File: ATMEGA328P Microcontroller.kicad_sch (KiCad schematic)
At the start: 25 parts, among them U1 24LC1025, U2 24LC1025, U3 ATmega328-P, U4 DS1337S_T_R, Y1 32.768 kHz, Y2 16MHz

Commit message: Wiring complete
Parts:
- BT1: footprint Connector_PinHeader_2.54mm:PinHeader_1x02_P2.54mm_Vertical -> (none)
- C1, C2, C3, C4, C5: footprint Capacitor_SMD:C_0805_2012Metric_Pad1.18x1.45mm_HandSolder -> (none)
- D1, D2: footprint LED_SMD:LED_0805_2012Metric -> (none)
- H1, H2, H3, H4: footprint MountingHole:MountingHole_2.1mm -> (none)
- R: renamed from R5; footprint Resistor_SMD:R_0805_2012Metric -> (none)
- R1, R2, R3, R4, R6, R7: footprint Resistor_SMD:R_0805_2012Metric -> (none)
- U1, U2: footprint Package_SO:SOIC-8_5.23x5.23mm_P1.27mm -> (none)
- Y1, Y2: footprint Crystal:Crystal_SMD_5032-2Pin_5.0x3.2mm_HandSoldering -> (none)
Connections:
- net GND: now also BT1.2 (-), C1.1, C2.1, C3.2, C4.2, C5.2, R.1, R4.2, U2.2 (A1), U2.4 (GND), U2.7 (WP), U3.22 (GND), U3.8 (GND)
- net at D1.1 (K): now also R.2
- net SCK: now reaches D1.2 (A)
- net SCK: now also R1.2, U1.6 (SCL), U2.6 (SCL), U3.19 (PB5), U3.28 (PC5), U4.6 (SCL)
- net Vcc: now reaches R1.1
- net Vcc: now also C3.1, R2.1, R3.1, R6.1, R7.1, U1.1 (A0), U1.2 (A1), U1.3 (A2), U1.8 (VCC), U2.1 (A0), U2.3 (A2), U2.8 (VCC), U4.8 (VCC)
- net at C1.2: now also U3.9 (XTAL1/PB6), Y2.1
- net SDA: now reaches U1.5 (SDA)
- net SDA: now also R2.2, U2.5 (SDA), U3.27 (PC4), U4.5 (SDA)
- net at D2.1 (K): now also R4.1
- net at D2.2 (A): now also BT1.1 (+), C5.1, U3.20 (AVCC), U3.7 (VCC)
- net at R6.2: now also U4.7 (SQW/~INT)
- net at Y2.2: now also C2.2, U3.10 (XTAL2/PB7)
- net at C4.1: now also U3.21 (AREF)
- net at U4.3 (~{INTA}): now also R3.2
- net RESET: now reaches R7.2
- net RESET: now also U3.1 (~{RESET}/PC6)
- net D4: now reaches U3.11 (PD5)
- net D5: now reaches U3.12 (PD6)
- net D6: now reaches U3.13 (PD7)
- net D7: now reaches U3.14 (PB0)
- net MOSI: now reaches U3.17 (PB3)
- net MISO: now reaches U3.18 (PB4)
- net RX: now reaches U3.2 (PD0)
- net TX: now reaches U3.3 (PD1)
- net D1: now reaches U3.4 (PD2)
- net D2: now reaches U3.5 (PD3)
- net D3: now reaches U3.6 (PD4)
- no-connect marks 0 -> 6
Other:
- moved on the sheet: BT1, C1, C2, C3, C4, C5, D1, D2, R, R3, R4, R6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

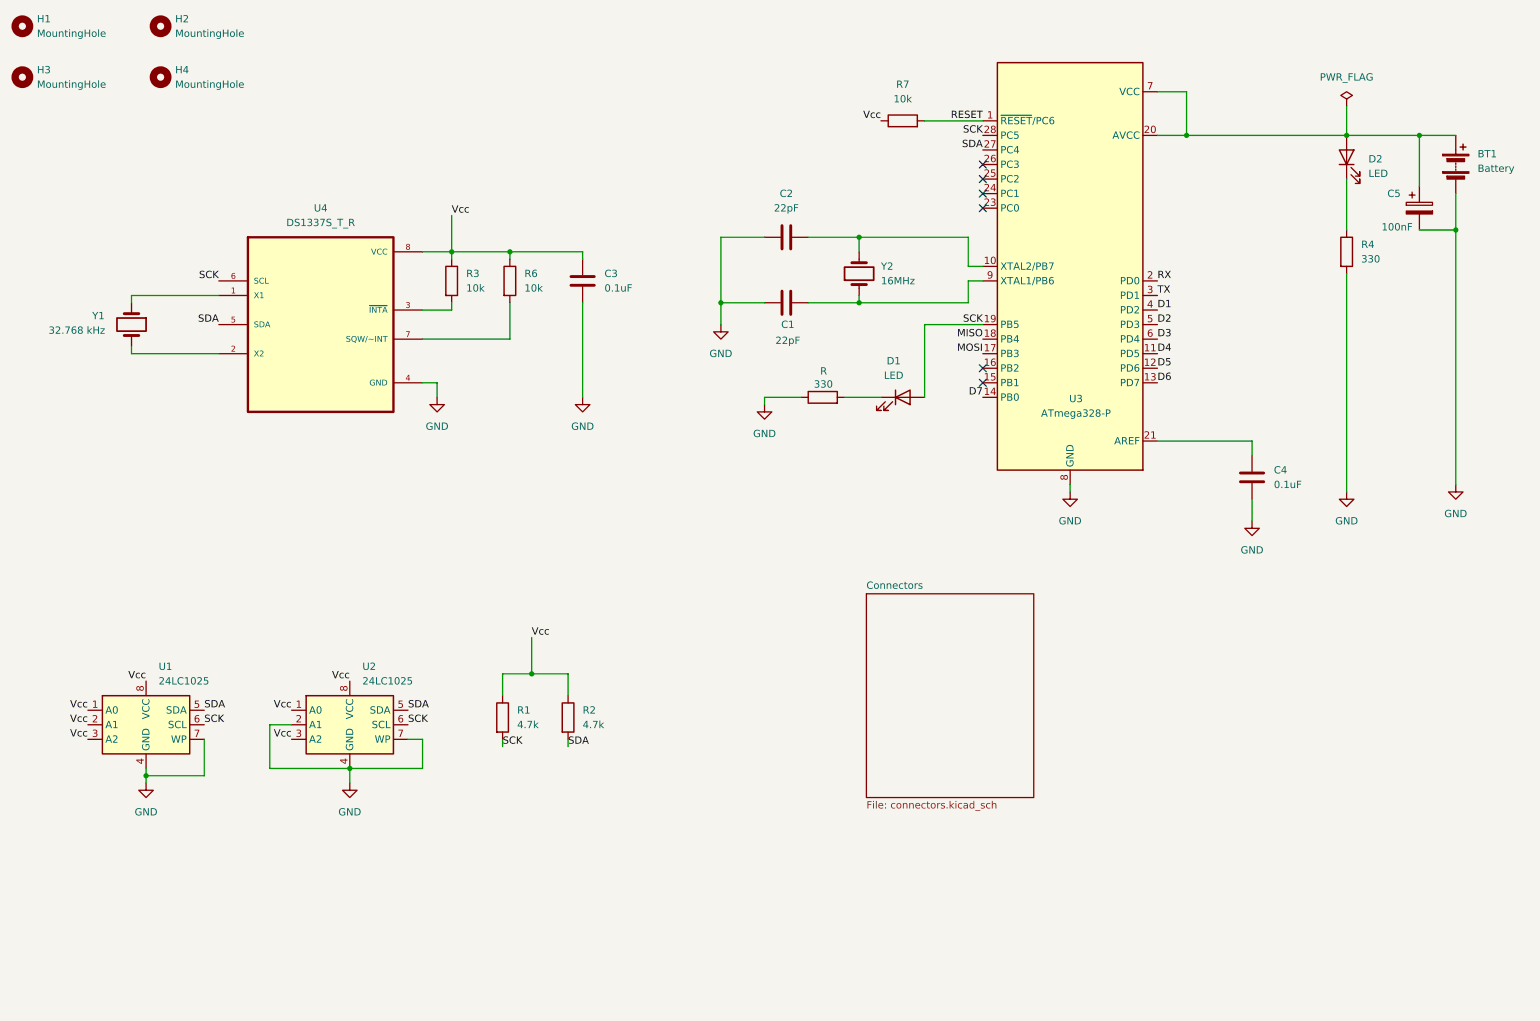
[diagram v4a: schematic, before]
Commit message: Allocated Vcc and GND nets to Power netclass
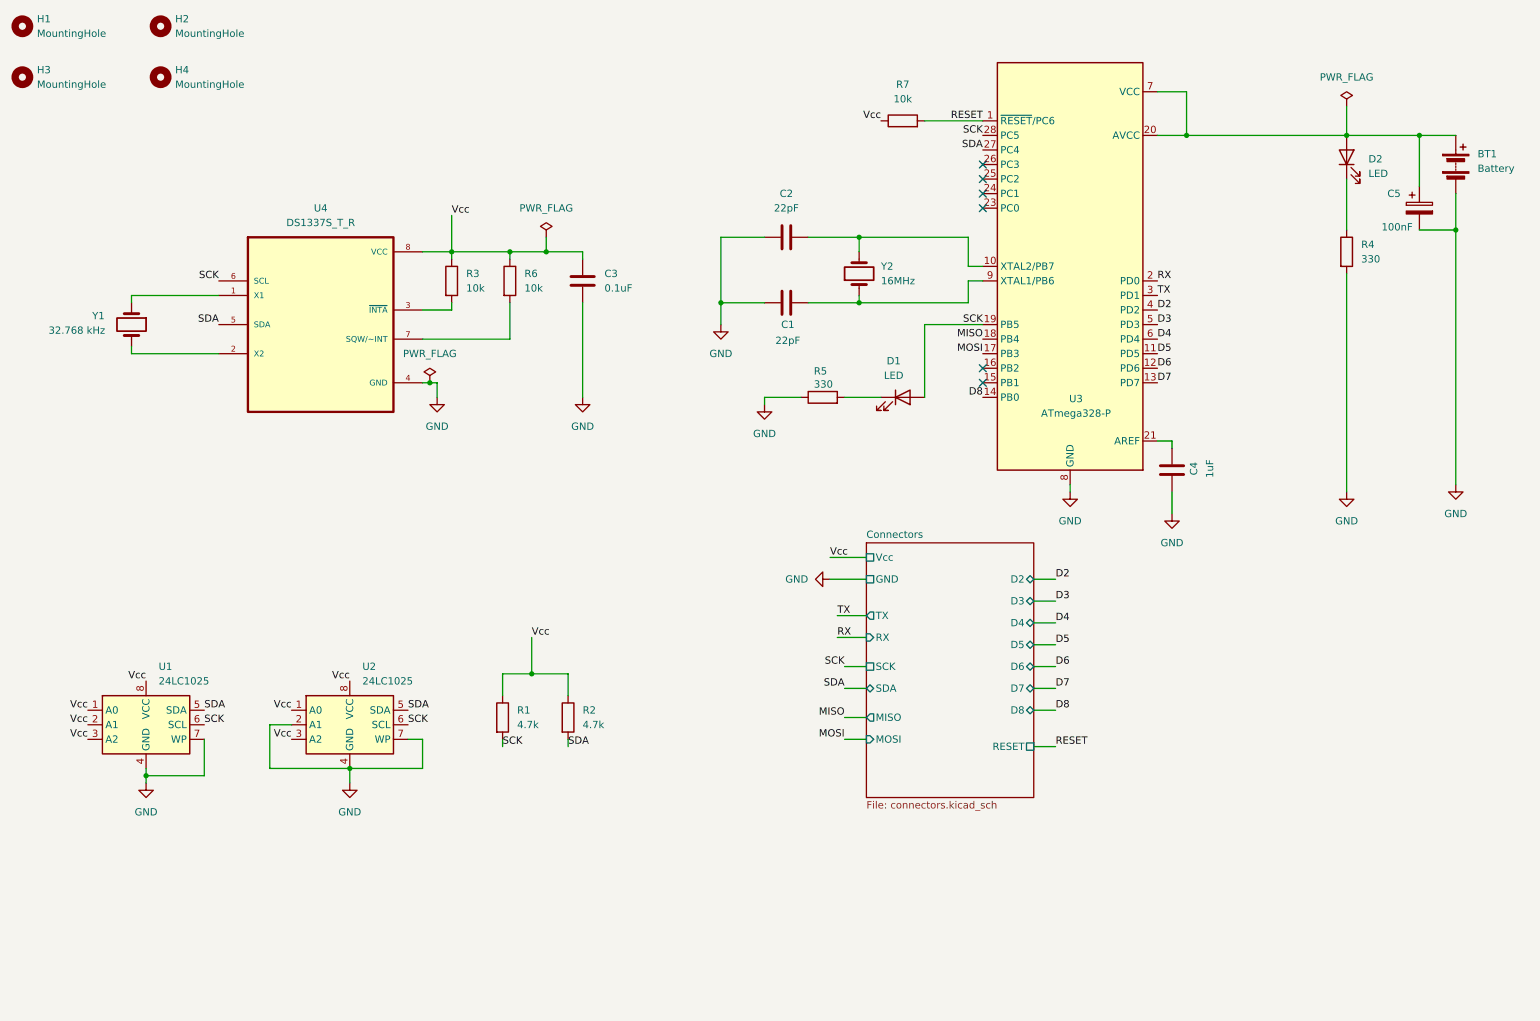
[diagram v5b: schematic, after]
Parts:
- C4: value 0.1uF -> 1uF
- renumbered R to R5
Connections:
- net D1 is gone; now on net D2: U3.4 (PD2)
- net D2: no longer U3.5 (PD3)
- net D3: now also U3.5 (PD3); no longer U3.6 (PD4)
- net D4: now also U3.6 (PD4); no longer U3.11 (PD5)
- net D5: now also U3.11 (PD5); no longer U3.12 (PD6)
- net D6: now also U3.12 (PD6); no longer U3.13 (PD7)
- net D7: now also U3.13 (PD7); no longer U3.14 (PB0)
- net GND: now also C4.1; no longer C4.2
- net at U3.21 (AREF): now also C4.2; no longer C4.1
- new net D8: U3.14 (PB0)
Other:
- sheet Connectors ports: added D2, D3, D4, D5, D6, D7, D8, GND, MISO, MOSI, RESET, RX, SCK, SDA, TX, Vcc; removed none

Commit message: Added comments to schematic
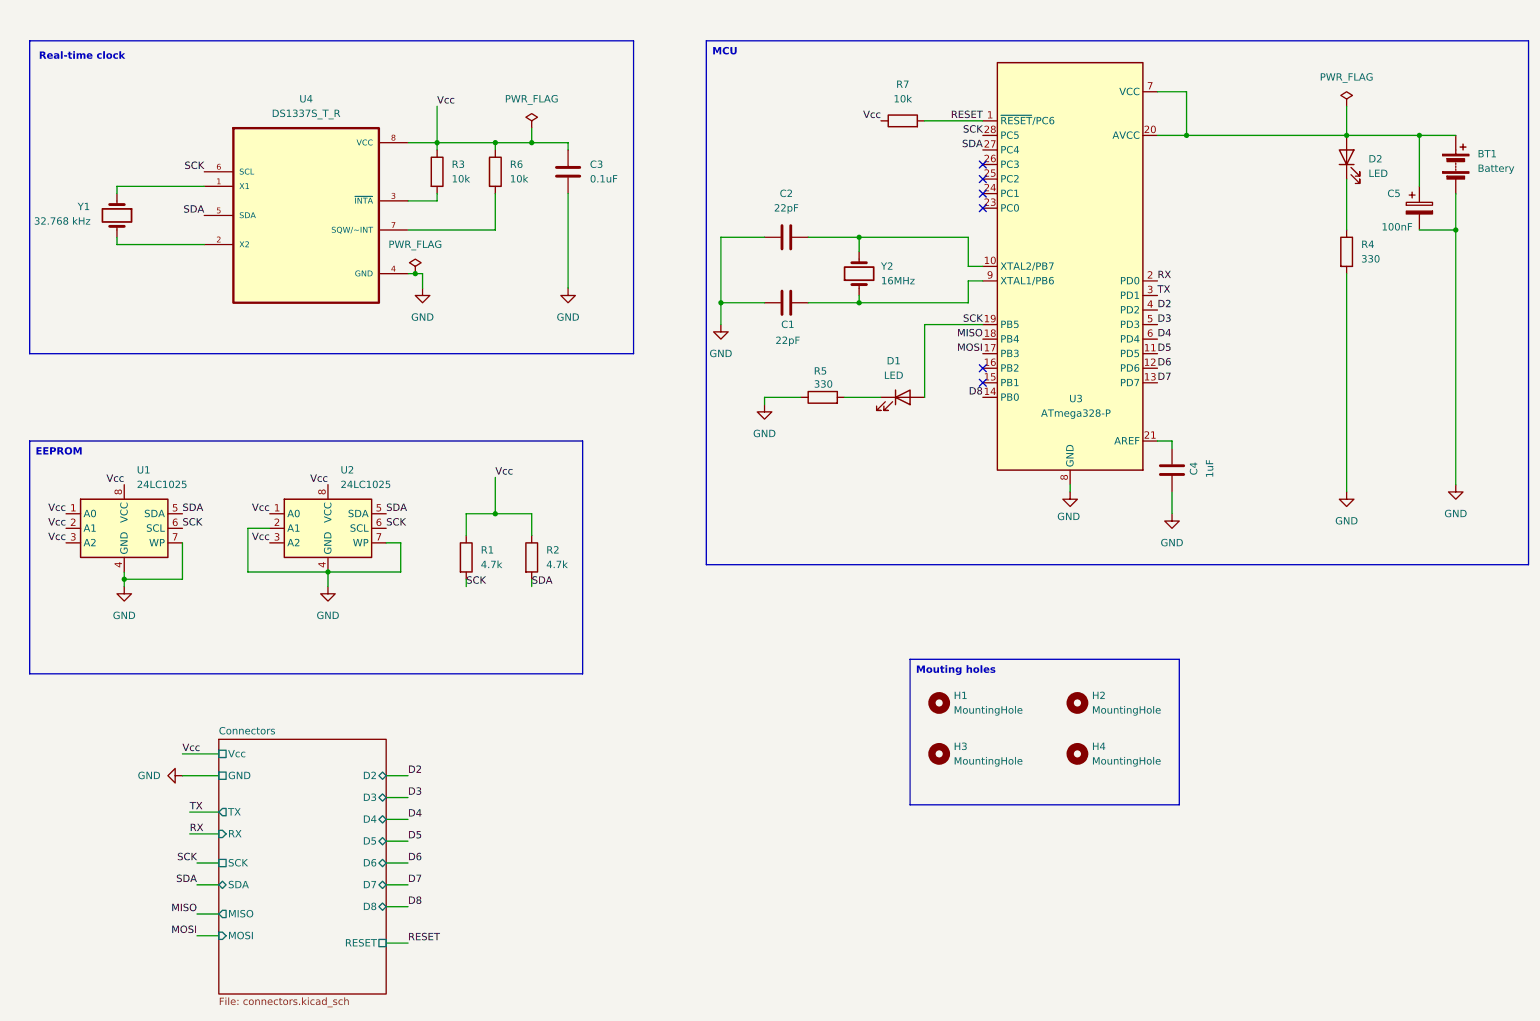
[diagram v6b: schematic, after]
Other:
- note added: "Real-time clock"
- moved on the sheet: C3, H1, H2, H3, H4, R1, R2, R3, R6, U1, U2, U4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

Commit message: Placed footprints on layout
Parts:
- BT1: footprint (none) -> Connector_PinHeader_2.54mm:PinHeader_1x02_P2.54mm_Vertical
- C1, C2, C3, C4, C5: footprint (none) -> Capacitor_SMD:C_0805_2012Metric
- D1, D2: footprint (none) -> LED_SMD:LED_0805_2012Metric
- H1, H2, H3, H4: footprint (none) -> MountingHole:MountingHole_2.2mm_M2
- R1, R2, R3, R4, R5, R6, R7: footprint (none) -> Resistor_SMD:R_0805_2012Metric
- U1, U2: footprint (none) -> Package_SO:SOIC-8_5.23x5.23mm_P1.27mm
- Y1, Y2: footprint (none) -> Crystal:Crystal_SMD_0603-2Pin_6.0x3.5mm_HandSoldering
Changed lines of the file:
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@@
 			)
 		)
-		(property "Footprint" ""
+		(property "Footprint" "Crystal:Crystal_SMD_0603-2Pin_6.0x3.5mm_HandSoldering"
 			(at 36.83 53.34 0)
 			(effects
@@
 			)
 		)
-		(property "Footprint" ""
+		(property "Footprint" "LED_SMD:LED_0805_2012Metric"
 			(at 173.99 85.09 0)
 			(effects
@@
 			)
 		)
-		(property "Footprint" ""
+		(property "Footprint" "Resistor_SMD:R_0805_2012Metric"
 			(at 96.012 113.03 90)
 			(effects
@@
 			)
 		)
-		(property "Footprint" ""
+		(property "Footprint" "Capacitor_SMD:C_0805_2012Metric"
 			(at 157.48 67.6148 0)
 			(effects
@@
 			)
 		)
-		(property "Footprint" ""
+		(property "Footprint" "Package_SO:SOIC-8_5.23x5.23mm_P1.27mm"
 			(at 38.1 107.95 0)
 			(effects
@@
 			)
 		)
-		(property "Footprint" ""
+		(property "Footprint" "MountingHole:MountingHole_2.2mm_M2"
 			(at 204.47 138.43 0)
 			(effects
@@
 			)
 		)
-		(property "Footprint" ""
+		(property "Footprint" "LED_SMD:LED_0805_2012Metric"
 			(at 251.46 43.18 0)
 			(effects
@@
 			)
 		)
-		(property "Footprint" ""
+		(property "Footprint" "Capacitor_SMD:C_0805_2012Metric"
 			(at 265.1252 55.88 0)
 			(effects
@@
 			)
 		)
-		(property "Footprint" ""
+		(property "Footprint" "Resistor_SMD:R_0805_2012Metric"
 			(at 160.02 86.868 90)
 			(effects
@@
 			)
 		)
-		(property "Footprint" ""
+		(property "Footprint" "Capacitor_SMD:C_0805_2012Metric"
 			(at 116.5352 49.53 0)
 			(effects
@@
 			)
 		)
-		(property "Footprint" ""
+		(property "Footprint" "Resistor_SMD:R_0805_2012Metric"
 			(at 101.092 45.72 90)
 			(effects
@@
 			)
 		)
-		(property "Footprint" ""
+		(property "Footprint" "Crystal:Crystal_SMD_0603-2Pin_6.0x3.5mm_HandSoldering"
 			(at 166.37 63.5 0)
 			(effects
@@
 			)
 		)
-		(property "Footprint" ""
+		(property "Footprint" "Resistor_SMD:R_0805_2012Metric"
 			(at 249.682 59.69 90)
 			(effects
@@
 			)
 		)
-		(property "Footprint" ""
+		(property "Footprint" "Resistor_SMD:R_0805_2012Metric"
 			(at 90.932 45.72 90)
 			(effects
@@
 			)
 		)
-		(property "Footprint" ""
+		(property "Footprint" "Capacitor_SMD:C_0805_2012Metric"
 			(at 157.48 56.1848 0)
 			(effects
@@
 			)
 		)
-		(property "Footprint" ""
+		(property "Footprint" "Resistor_SMD:R_0805_2012Metric"
 			(at 107.442 113.03 90)
 			(effects
@@
 			)
 		)
-		(property "Footprint" ""
+		(property "Footprint" "Package_SO:SOIC-8_5.23x5.23mm_P1.27mm"
 			(at 73.66 107.95 0)
 			(effects
@@
 			)
 		)
-		(property "Footprint" ""
+		(property "Footprint" "MountingHole:MountingHole_2.2mm_M2"
 			(at 180.34 147.32 0)
 			(effects
@@
 			)
 		)
-		(property "Footprint" ""
+		(property "Footprint" "MountingHole:MountingHole_2.2mm_M2"
 			(at 204.47 147.32 0)
 			(effects
@@
 			)
 		)
-		(property "Footprint" ""
+		(property "Footprint" "Resistor_SMD:R_0805_2012Metric"
 			(at 173.99 38.608 90)
 			(effects
@@
 			)
 		)
-		(property "Footprint" ""
+		(property "Footprint" "MountingHole:MountingHole_2.2mm_M2"
 			(at 180.34 138.43 0)
 			(effects
@@
 			)
 		)
-		(property "Footprint" ""
+		(property "Footprint" "Capacitor_SMD:C_0805_2012Metric"
 			(at 220.0148 93.98 0)
 			(effects
@@
 			)
 		)
-		(property "Footprint" ""
+		(property "Footprint" "Connector_PinHeader_2.54mm:PinHeader_1x02_P2.54mm_Vertical"
 			(at 270.51 42.926 90)
 			(effects
